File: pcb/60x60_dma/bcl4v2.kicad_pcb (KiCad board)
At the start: 2 copper layers, 60 x 60 mm, 51 parts, among them J1 Conn_01x05, J10 Conn_01x01_Female, J11 Conn_01x01_Female, J12 Conn_01x01_Female, J13 Conn_01x01_Female, J14 Conn_01x02, J15 Conn_01x04, J2 Conn_01x05, J3 USB_OTG, J4 Conn_01x05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

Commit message: - just before autoroute
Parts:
- added D6: LED_MATRIX_8x8, kicad_libraries_new:badger_LED_MATRIX_8x8_60.2mmx60.2mm, F.Cu at (100.0, 100.0)
- moved R3 14.5 mm to (116.4, 82.0), turned to 0 degrees
- moved U3 13.1 mm to (105.3, 100.6)
- moved U5 8.15 mm to (105.1, 88.2), turned to 90 degrees
- moved U4 7.96 mm to (97.1, 113.2)
- moved R5 2.25 mm to (116.5, 79.8)
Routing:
- net /USB_D+: track 0.00 -> 37.9 mm, vias 0 -> 2
- net /USB_D-: track 0.00 -> 37.6 mm, vias 0 -> 2
- removed copper zone on B.Cu, net GND
- removed copper zone on F.Cu, net GND
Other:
- board text added: "BTN0"
- board text added: "BTN1"
- board text added: "IN0"
- board text added: "IN1"
- board text added: "IN2"
- board text added: "IN3"
- board text added: "RX1"
- board text added: "RX2"
- board text added: "RX3"
- board text added: "RX4"
- board text added: "SCL"
- board text added: "SDA"
- board text added: "TX1"
- board text added: "TX2"
- board text added: "TX3"
- board text added: "TX4"
- board text added: "VCC"
- board text removed: "GND VCC"

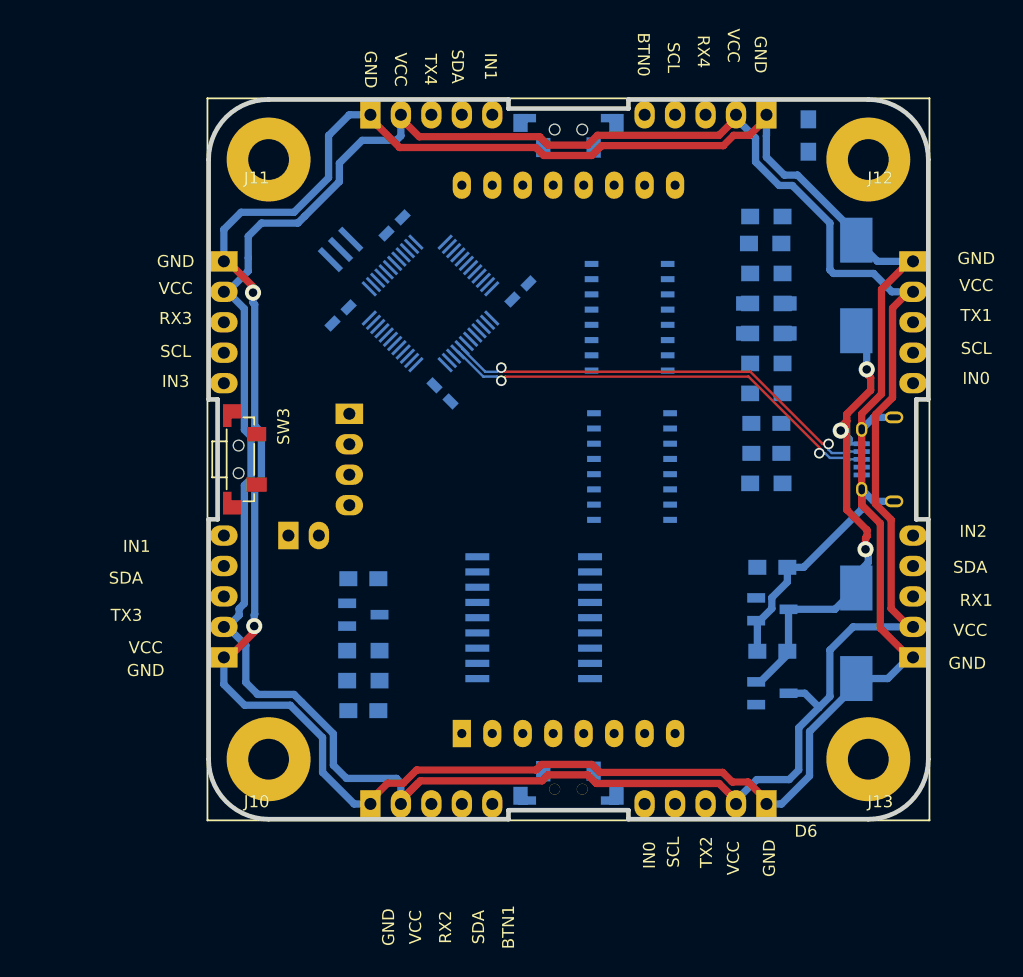
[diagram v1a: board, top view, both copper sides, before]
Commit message: - add 60x60_dma version
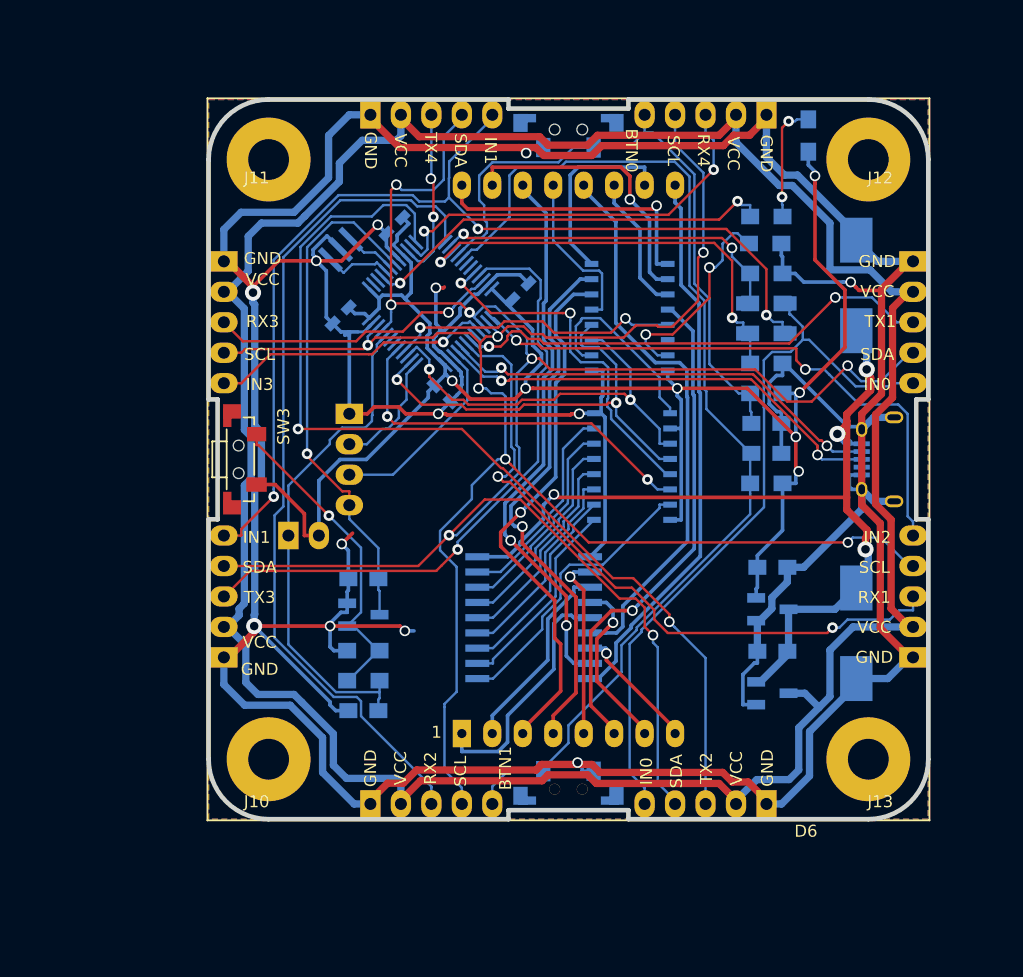
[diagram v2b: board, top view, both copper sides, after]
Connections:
- J4 pad 4: /I2C_SCL -> /I2C_SDA
- J5 pad 4: /I2C_SDA -> /I2C_SCL
- J8 pad 4: /I2C_SCL -> /I2C_SDA
- J9 pad 4: /I2C_SDA -> /I2C_SCL
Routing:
- net GND: track 250.9 -> 430.5 mm, vias 2 -> 13
- net /I2C_SDA: track 0.00 -> 152.9 mm, vias 0 -> 7
- net +3V3: track 0.00 -> 152.7 mm, vias 0 -> 7
- net /I2C_SCL: track 0.00 -> 146.8 mm, vias 0 -> 6
- net /BTN1: track 0.00 -> 90.0 mm
- net /IN1P: track 0.00 -> 87.2 mm, vias 0 -> 3
- net /UART_TX2: track 0.00 -> 83.4 mm, vias 0 -> 2
- net /UART_RX2: track 0.00 -> 70.6 mm
- net /IN0P: track 0.00 -> 61.1 mm
- net /UART_RX1: track 0.00 -> 57.3 mm, vias 0 -> 2
- net /BTN0: track 0.00 -> 53.9 mm
- net /UART_TX3: track 0.00 -> 52.8 mm, vias 0 -> 1
- net /IN2: track 0.00 -> 48.9 mm, vias 0 -> 2
- net /LED_matrix/OUT_A3: track 0.00 -> 46.8 mm
- net /LED_matrix/OUT_A1: track 0.00 -> 46.5 mm, vias 0 -> 2
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- added copper zone on B.Cu, net GND
- added copper zone on F.Cu, net GND
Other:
- board text added: "1"
- board text added: "R3 sets matrix brightness"
- board text added: "rev 0.4"
- board text removed: "SW3 <1s reset >3s bootloader"
- board text removed: "TODO: add header comments"
- board text removed: "rev 0.2"

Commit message: - fix display connections, add testpoints
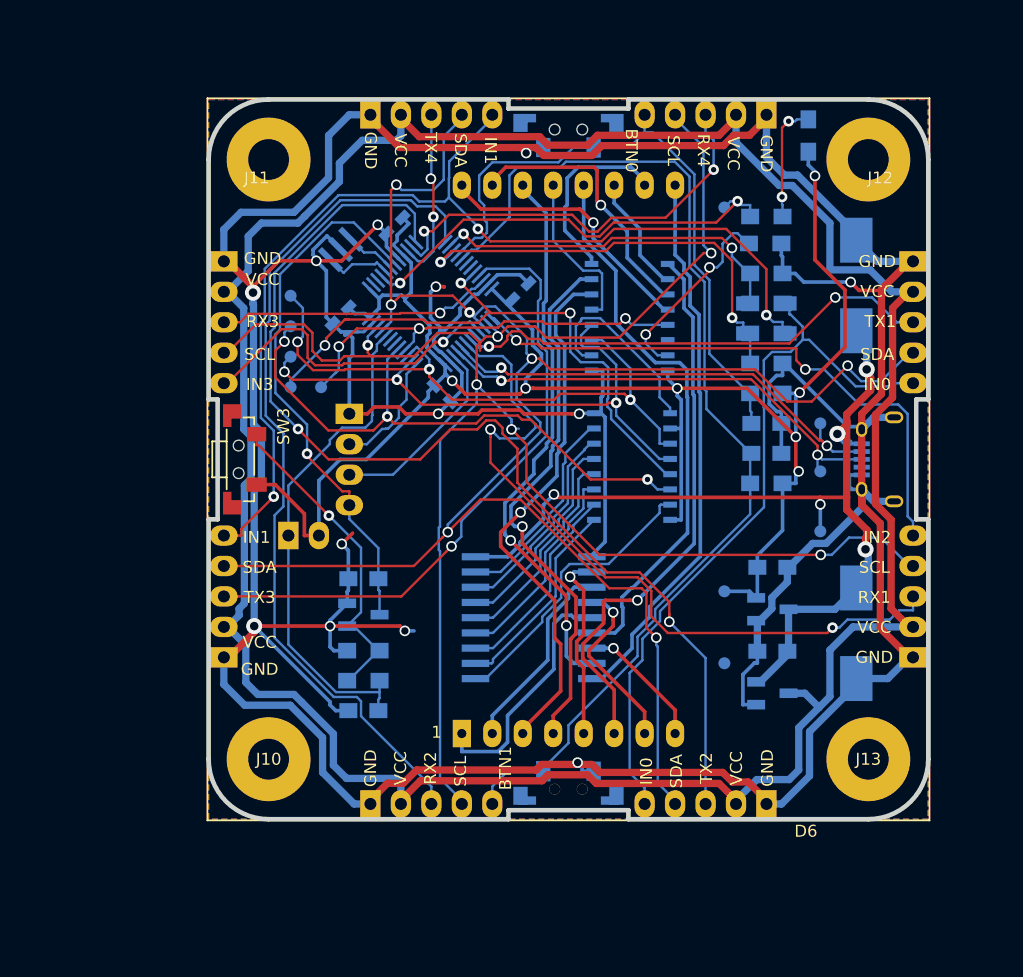
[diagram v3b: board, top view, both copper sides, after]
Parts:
- added 3V3: TestPoint, TestPoint:TestPoint_Pad_D1.0mm, B.Cu at (113.0, 111.0)
- added 5V: TestPoint, TestPoint:TestPoint_Pad_D1.0mm, B.Cu at (121.0, 106.0)
- added AnOE: TestPoint, TestPoint:TestPoint_Pad_D1.0mm, B.Cu at (76.8, 94.0)
- added CnOE: TestPoint, TestPoint:TestPoint_Pad_D1.0mm, B.Cu at (79.4, 94.0)
- added D+: TestPoint, TestPoint:TestPoint_Pad_D1.0mm, B.Cu at (121.0, 101.0)
- added D-: TestPoint, TestPoint:TestPoint_Pad_D1.0mm, B.Cu at (121.0, 97.0)
- added DCLK: TestPoint, TestPoint:TestPoint_Pad_D1.0mm, B.Cu at (76.8, 86.4)
- added DDATA: TestPoint, TestPoint:TestPoint_Pad_D1.0mm, B.Cu at (76.8, 88.9)
- added DSTRB: TestPoint, TestPoint:TestPoint_Pad_D1.0mm, B.Cu at (76.8, 91.4)
- added GND: TestPoint, TestPoint:TestPoint_Pad_D1.0mm, B.Cu at (113.0, 117.0)
- added TP6: TestPoint, TestPoint:TestPoint_Pad_D1.0mm, B.Cu at (113.0, 79.0)
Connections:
- J3 pad 4: (no net) -> Net-(J3-Pad4)
- U2 pad 18: (no net) -> Net-(U2-Pad18)
- U2 pad 19: (no net) -> Net-(U2-Pad19)
- U2 pad 2: (no net) -> Net-(U2-Pad2)
- U2 pad 29: (no net) -> Net-(U2-Pad29)
- U2 pad 3: (no net) -> Net-(U2-Pad3)
- U2 pad 42: (no net) -> Net-(U2-Pad42)
- U2 pad 43: (no net) -> Net-(U2-Pad43)
- U5 pad 10: /LED_matrix/OUT_C6 -> /LED_matrix/OUT_C5
- U5 pad 11: /LED_matrix/OUT_C5 -> /LED_matrix/OUT_C6
- U5 pad 12: /LED_matrix/OUT_C4 -> /LED_matrix/OUT_C7
- U5 pad 14: (no net) -> Net-(U5-Pad14)
- U5 pad 9: /LED_matrix/OUT_C7 -> /LED_matrix/OUT_C4
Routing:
- net /AN_NOE: track 29.9 -> 51.1 mm, vias 2 -> 3
- net /DISP_DATA: track 32.2 -> 49.2 mm, vias 2 -> 3
- net /DISP_CLK: track 34.7 -> 51.4 mm, vias 2 -> 3
- net /CAT_NOE: track 24.6 -> 35.7 mm, vias 2 -> 3
- net /DISP_STROBE: track 37.5 -> 48.3 mm, vias 2 -> 3
- net /I2C_SCL: track 146.8 -> 154.7 mm
- net /UART_TX2: track 83.4 -> 90.5 mm
- net /UART_RX1: track 57.3 -> 62.1 mm
- net /LED_matrix/OUT_C4: track 41.8 -> 46.6 mm
- net /IN3: track 24.5 -> 28.1 mm
- net +5V: track 75.6 -> 78.4 mm, vias 4 -> 5
- net +3V3: track 152.7 -> 155.2 mm
- net /LED: track 35.0 -> 37.5 mm
- net /I2C_SDA: track 152.9 -> 155.3 mm
- net /NRST: track 43.0 -> 45.2 mm
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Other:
- rule pad_to_mask_clearance: 0.254 -> 0.0508
- board text added: "SW3 <1s reset >3s bootloader"
- board text added: "TODO: add open hardware logo"
- board text added: "rev 0.5"
- board text removed: "rev 0.4"

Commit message: - add LSE crystal (needs to fix routing and zones)
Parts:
- added C14: 2pF, kicad_lib:badger_C_0603_HandSoldering, B.Cu at (77.8, 83.0)
- added C15: 2pF, kicad_lib:badger_C_0603_HandSoldering, B.Cu at (78.9, 81.9)
- added Y2: ABS07-120-32.768kHz-T, kicad_lib:badger_crystal_ABS07-120-xx_handsolder, B.Cu at (80.6, 84.5)
- U4: footprint Housings_SOIC:SOIC-18W_7.5x11.6mm_Pitch1.27mm -> kicad_lib:badger_SOIC-18W_7.5x11.6mm_Pitch1.27mm
- moved Y1 2.87 mm to (82.5, 80.1)
- moved C6 1.15 mm to (86.5, 79.9)
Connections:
- U2 pad 2: Net-(U2-Pad2) -> /LED
- U2 pad 3: Net-(U2-Pad3) -> /LSE_IN
- U2 pad 4: /LED -> /LSE_OUT
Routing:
- net /IN1P: track 88.9 -> 118.3 mm, vias 3 -> 4
- net /UART_RX2: track 71.8 -> 84.2 mm, vias 0 -> 2
- net /UART_TX2: track 90.5 -> 78.3 mm, vias 2 -> 4
- net /LSE_IN: track 0.00 -> 7.33 mm
- net GND: track 431.0 -> 437.9 mm, vias 13 -> 12
- net /LSE_OUT: track 0.00 -> 5.73 mm
- net /UART_RX1: track 62.1 -> 57.7 mm
- net /I2C_SCL: track 154.7 -> 151.9 mm
- net /OSC_OUT: track 4.29 -> 6.18 mm
- net +5V: track 78.4 -> 80.3 mm
- net /NRST: track 45.2 -> 43.5 mm, vias 1 -> 3
- net /I2C_SDA: track 155.3 -> 154.1 mm
- net /LED_matrix/OUT_C7: track 22.5 -> 23.6 mm
- net /LED: track 37.5 -> 38.6 mm
- net +3V3: track 155.2 -> 156.3 mm
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
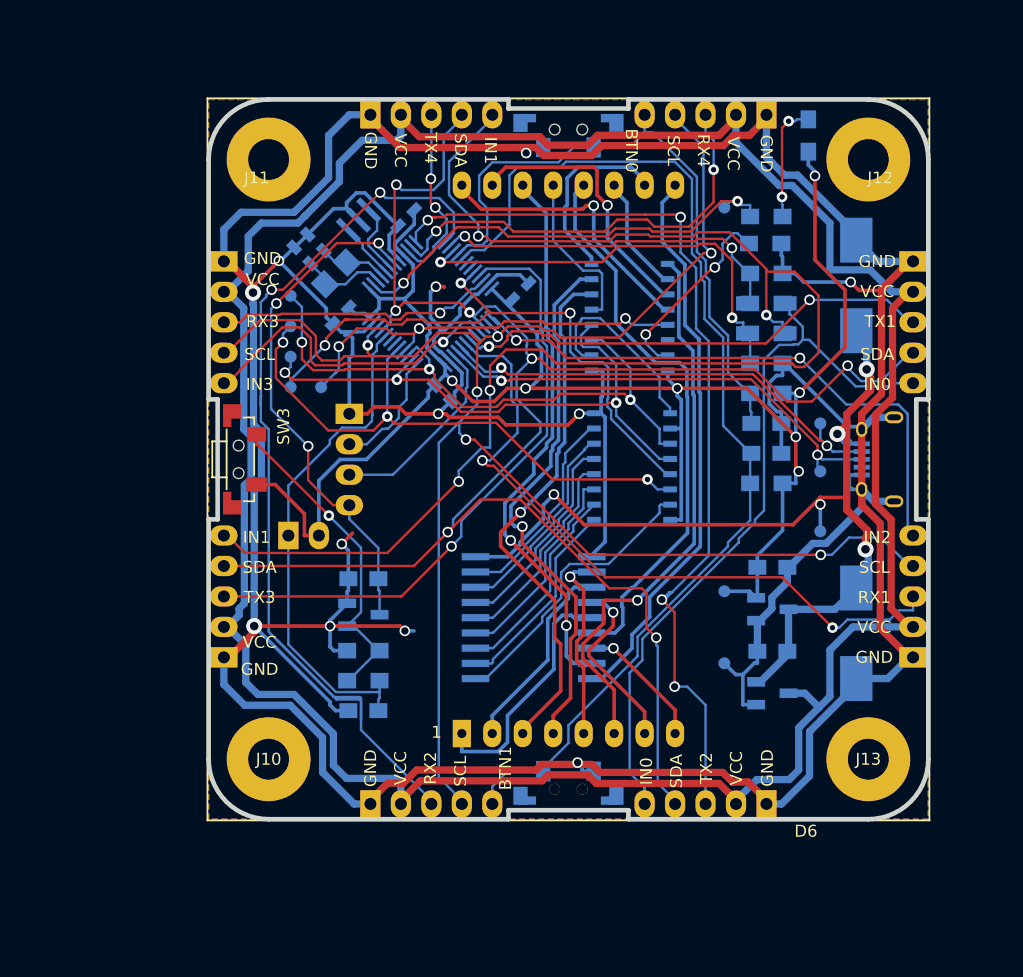
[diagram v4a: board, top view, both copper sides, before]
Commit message: - larger USB pads, larger switch cuts, silk fixes
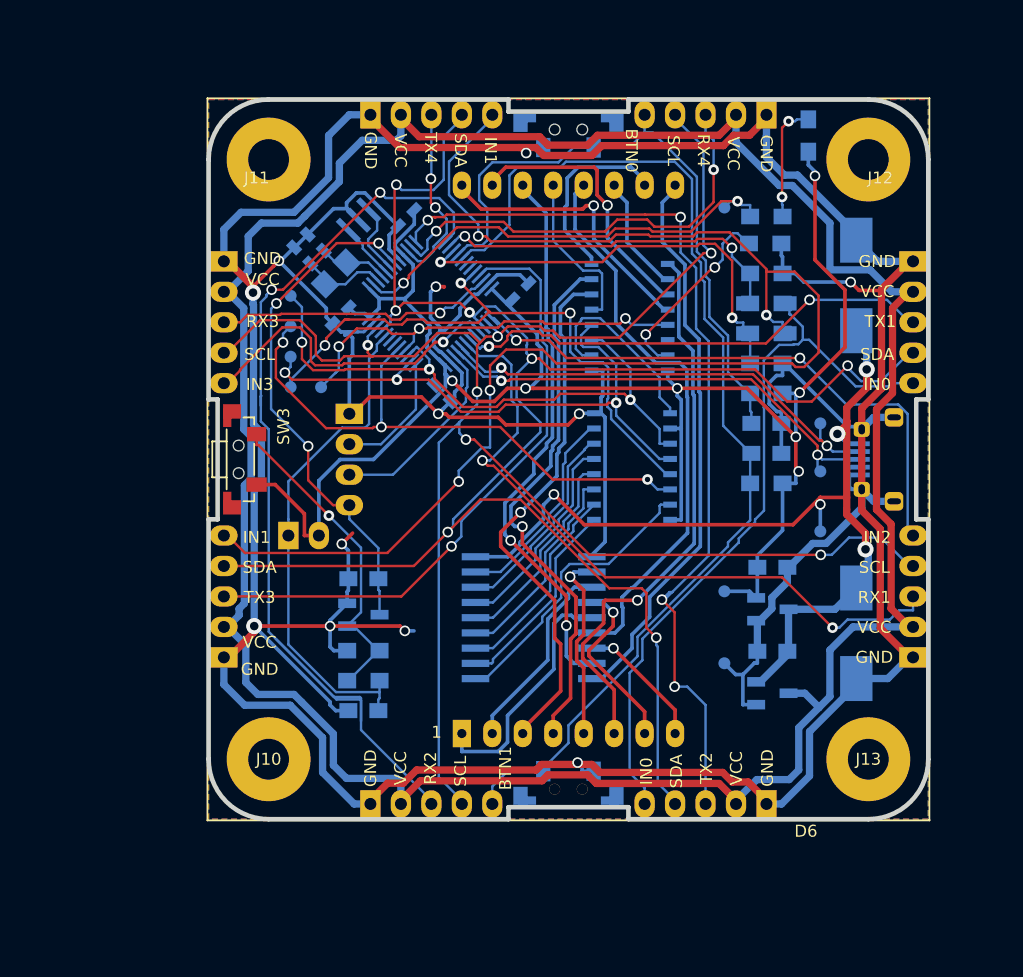
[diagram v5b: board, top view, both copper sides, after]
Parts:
- J3: footprint Connect:USB_Micro-B -> kicad_libraries_new:badger_USB_Micro-B_handsolder
- U2: footprint kicad_libraries_new:badger_LQFP-48_7x7mm_Pitch0.5mm_handsolder -> kicad_libraries_new:badger_LQFP-48_7x7mm_Pitch0.5mm_handsolder_pin1
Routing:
- net GND: track 437.9 -> 438.6 mm
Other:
- outline, holes or cut-outs redrawn
- board text added: "Y1 HSE for USB Y2 (C14,C15) LSE for RTC"
- board text removed: "C6-9 optional, they are for better MCU power stability Y1 optional, e.g. USB needs it"

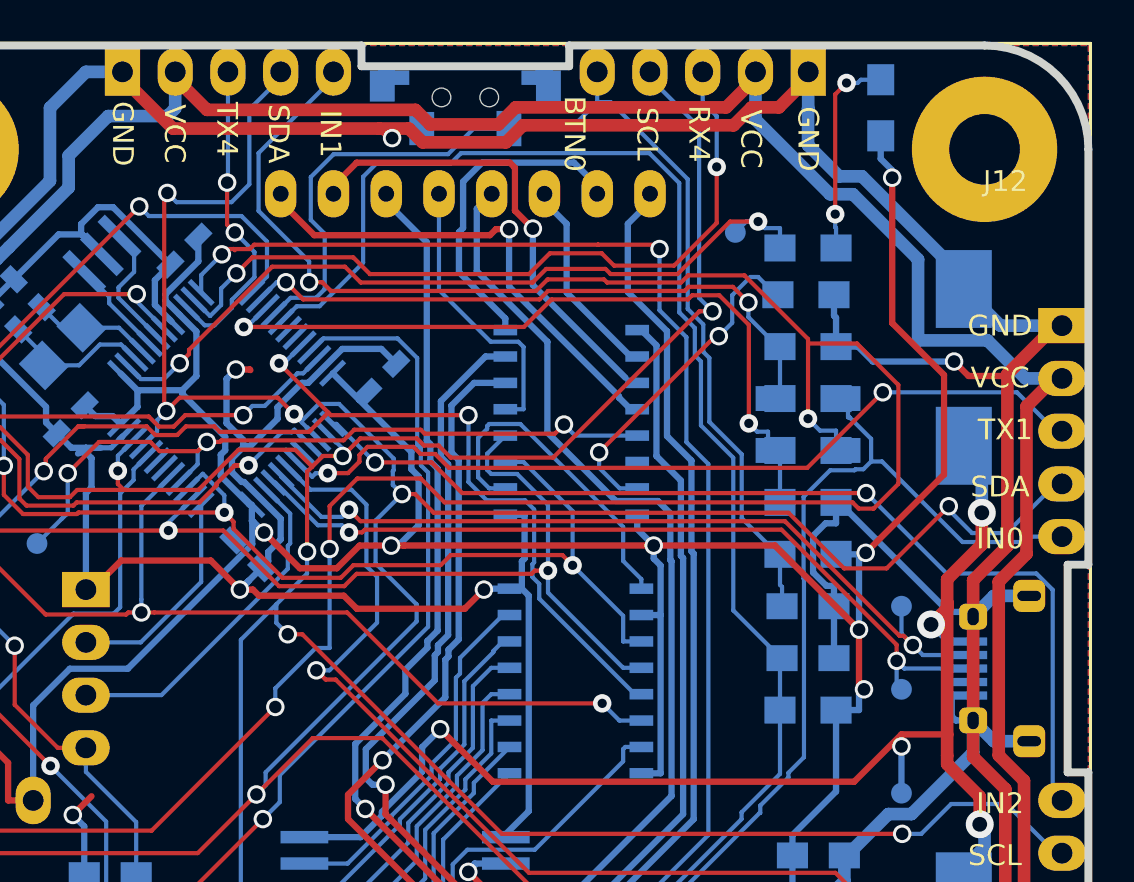
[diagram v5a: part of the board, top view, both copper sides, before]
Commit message: - add OSHV logo, move LED a bit
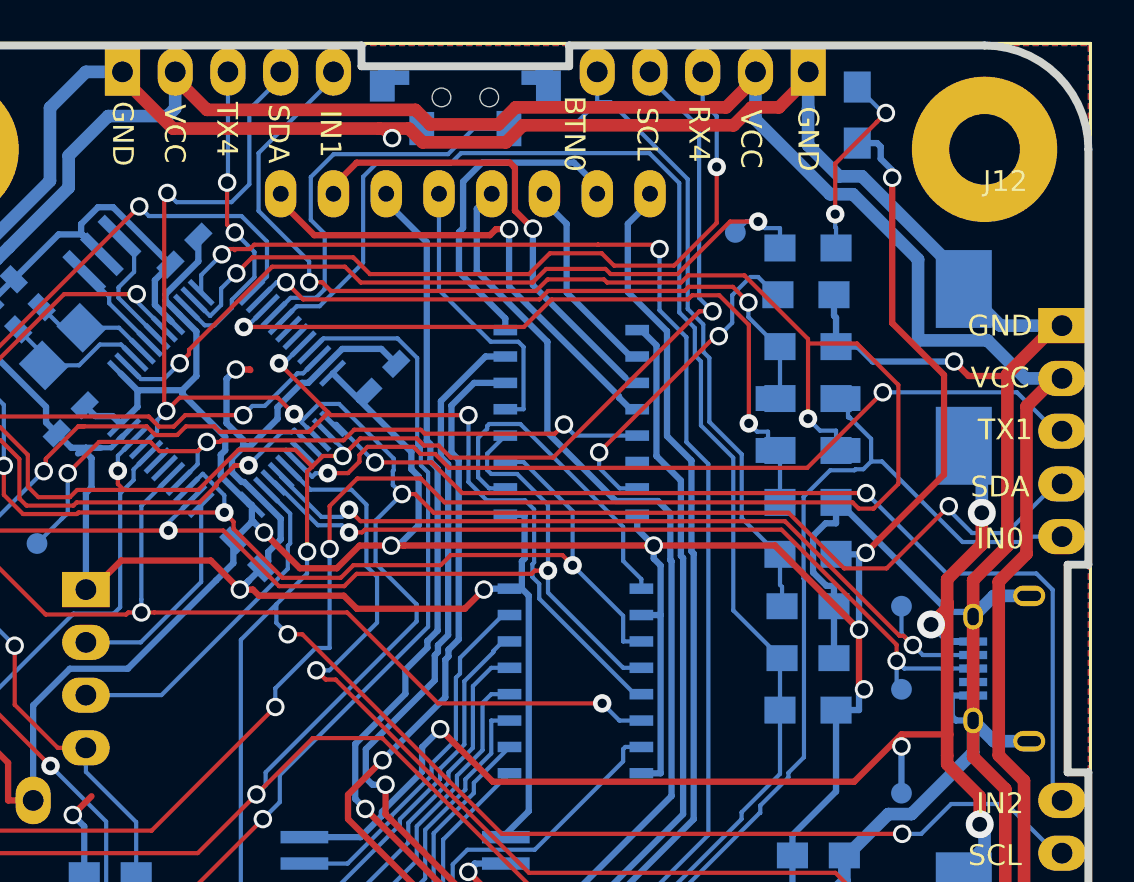
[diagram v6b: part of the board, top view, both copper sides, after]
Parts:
- added LOGO1: OSHW-LOGOM, kicad_libraries_new:OSHW-LOGO-M, B.Cu at (97.3, 96.2)
- D5: footprint LEDs:LED_0805_HandSoldering -> kicad_libraries_new:badger_LED_0805_HandSoldering
- J3: footprint kicad_libraries_new:badger_USB_Micro-B_handsolder -> Connect:USB_Micro-B
- R3: value 1k -> 470
- U2: footprint kicad_libraries_new:badger_LQFP-48_7x7mm_Pitch0.5mm_handsolder_pin1 -> kicad_libraries_new:badger_LQFP-48_7x7mm_Pitch0.5mm_handsolder
- moved D5 1.18 mm to (118.9, 73.3)
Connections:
- U5 pad 14: Net-(U5-Pad14) -> (no net)
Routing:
- net +3V3: track 156.6 -> 157.3 mm
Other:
- board text added: "(c)2019 Badger"
- board text added: "rev 0.6"
- board text removed: "(c)2018 Badger"
- board text removed: "rev 0.5"
